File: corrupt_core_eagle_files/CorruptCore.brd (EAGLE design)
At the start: 100 x 58 mm, 90 parts, among them K1 DTS-3, K10 DTS-3, K11 DTS-3, K12 DTS-3, K13 DTS-3, K14 DTS-3, K15 DTS-3, K16 DTS-3, K2 DTS-3, K3 DTS-3, K4 DTS-3, K5 DTS-3, K6 DTS-3, K7 DTS-3, K8 DTS-3, K9 DTS-3, U1 MEGA8-P, U2 SNX4HC595SOIC16, U3 SNX4HC595SOIC16, U4 SNX4HC595SOIC16, U5 ULN2803ASOIC18, U6 ULN2803ASOIC18, U7 ULN2803ASOIC18, U8 LTC1799, Y1 16MHz

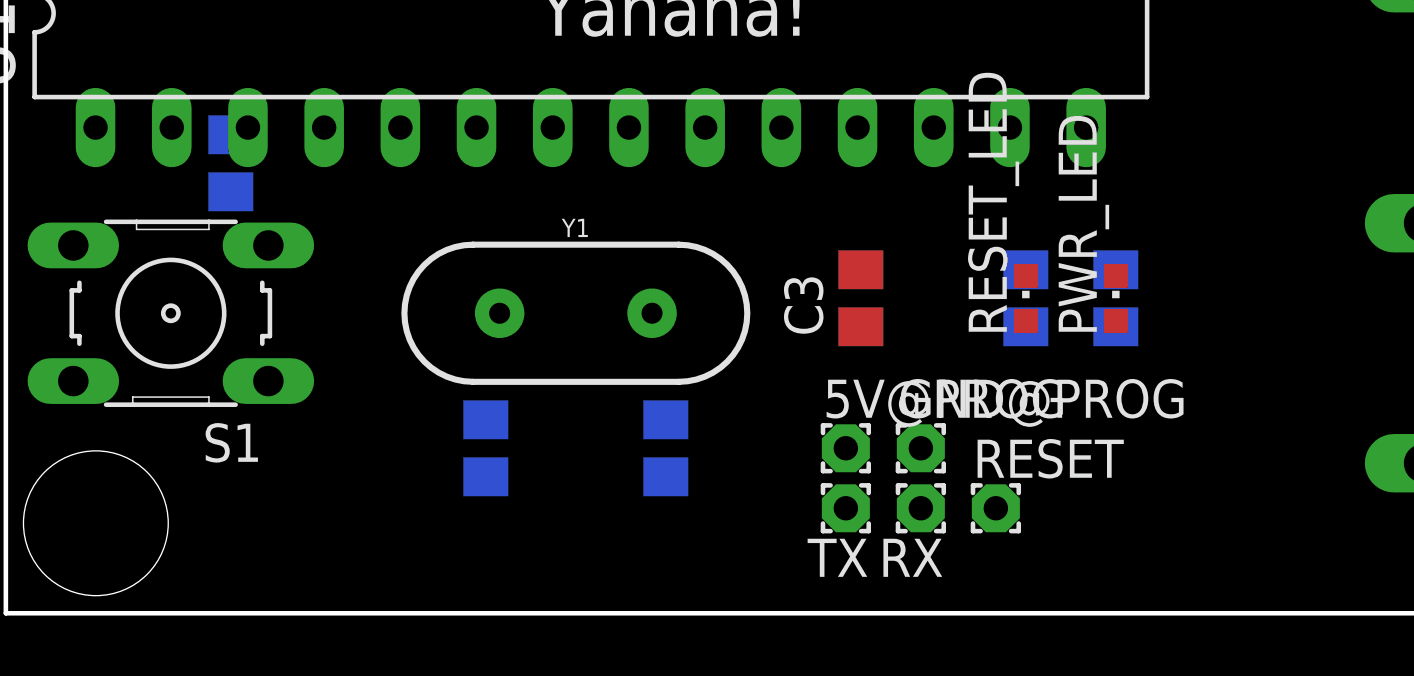
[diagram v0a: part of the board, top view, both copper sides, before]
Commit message: -starting to fix up the soldermask
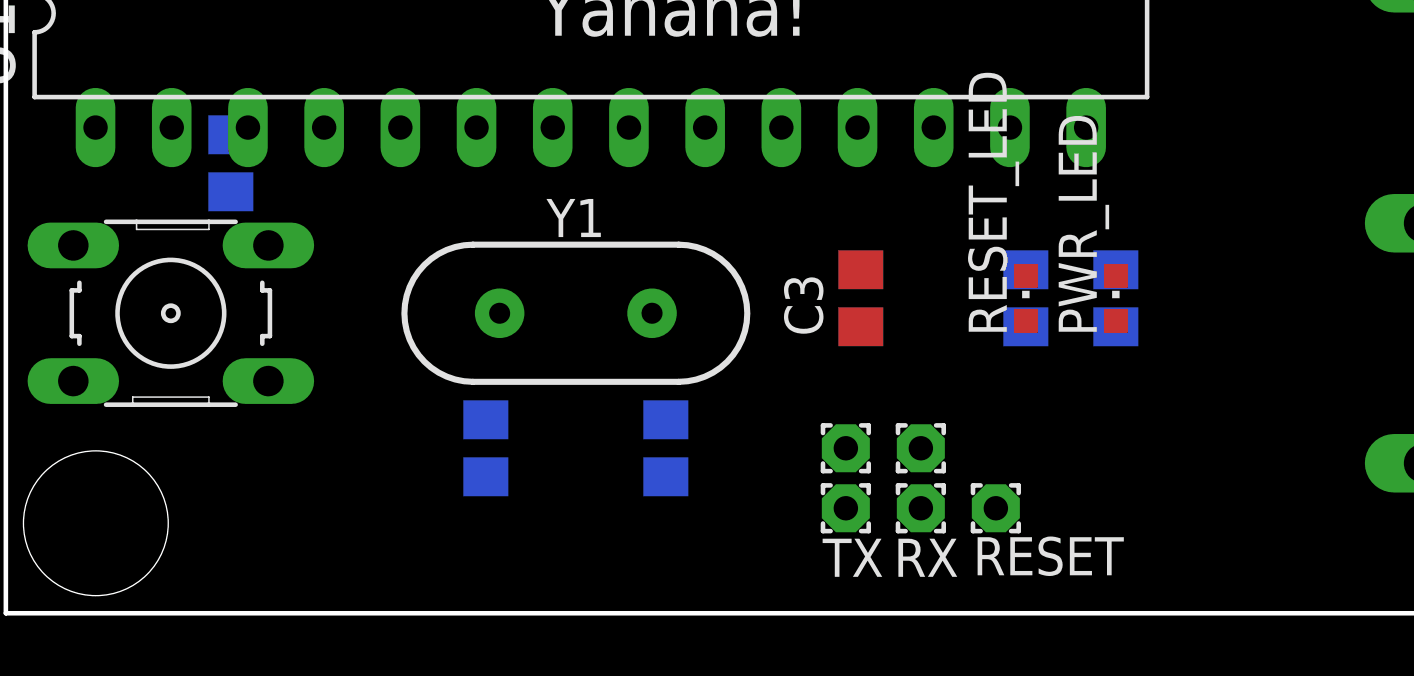
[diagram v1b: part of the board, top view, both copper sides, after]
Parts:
- 5V@PROG: value (none) -> 5V
- GND@PROG: value (none) -> GND
- S1: value (none) -> RESET
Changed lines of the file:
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@@
 <layer number="14" name="Route14" color="1" fill="6" visible="no" active="no"/>
 <layer number="15" name="Route15" color="4" fill="6" visible="no" active="no"/>
-<layer number="16" name="Bottom" color="1" fill="1" visible="yes" active="yes"/>
+<layer number="16" name="Bottom" color="1" fill="1" visible="no" active="yes"/>
 <layer number="17" name="Pads" color="2" fill="1" visible="yes" active="yes"/>
 <layer number="18" name="Vias" color="2" fill="1" visible="yes" active="yes"/>
@@
 <layer number="20" name="Dimension" color="15" fill="1" visible="yes" active="yes"/>
 <layer number="21" name="tPlace" color="7" fill="1" visible="yes" active="yes"/>
-<layer number="22" name="bPlace" color="7" fill="1" visible="yes" active="yes"/>
+<layer number="22" name="bPlace" color="7" fill="1" visible="no" active="yes"/>
 <layer number="23" name="tOrigins" color="15" fill="1" visible="yes" active="yes"/>
-<layer number="24" name="bOrigins" color="15" fill="1" visible="yes" active="yes"/>
+<layer number="24" name="bOrigins" color="15" fill="1" visible="no" active="yes"/>
 <layer number="25" name="tNames" color="7" fill="1" visible="yes" active="yes"/>
-<layer number="26" name="bNames" color="7" fill="1" visible="yes" active="yes"/>
+<layer number="26" name="bNames" color="7" fill="1" visible="no" active="yes"/>
 <layer number="27" name="tValues" color="7" fill="1" visible="yes" active="yes"/>
-<layer number="28" name="bValues" color="7" fill="1" visible="yes" active="yes"/>
+<layer number="28" name="bValues" color="7" fill="1" visible="no" active="yes"/>
 <layer number="29" name="tStop" color="7" fill="3" visible="no" active="yes"/>
 <layer number="30" name="bStop" color="7" fill="6" visible="no" active="yes"/>
@@
 <layer number="38" name="bTest" color="7" fill="1" visible="no" active="yes"/>
 <layer number="39" name="tKeepout" color="4" fill="11" visible="yes" active="yes"/>
-<layer number="40" name="bKeepout" color="1" fill="11" visible="yes" active="yes"/>
+<layer number="40" name="bKeepout" color="1" fill="11" visible="no" active="yes"/>
 <layer number="41" name="tRestrict" color="4" fill="10" visible="yes" active="yes"/>
-<layer number="42" name="bRestrict" color="1" fill="10" visible="yes" active="yes"/>
+<layer number="42" name="bRestrict" color="1" fill="10" visible="no" active="yes"/>
 <layer number="43" name="vRestrict" color="2" fill="10" visible="no" active="yes"/>
-<layer number="44" name="Drills" color="7" fill="1" visible="yes" active="yes"/>
+<layer number="44" name="Drills" color="7" fill="1" visible="no" active="yes"/>
 <layer number="45" name="Holes" color="7" fill="1" visible="yes" active="yes"/>
 <layer number="46" name="Milling" color="3" fill="1" visible="no" active="yes"/>
@@
 <layer number="50" name="dxf" color="7" fill="1" visible="no" active="no"/>
 <layer number="51" name="tDocu" color="7" fill="1" visible="yes" active="yes"/>
-<layer number="52" name="bDocu" color="7" fill="1" visible="yes" active="yes"/>
+<layer number="52" name="bDocu" color="7" fill="1" visible="no" active="yes"/>
 <layer number="53" name="tGND_GNDA" color="7" fill="9" visible="no" active="no"/>
 <layer number="54" name="bGND_GNDA" color="1" fill="9" visible="no" active="no"/>
@@
 </element>
 <element name="R1" library="resistor" library_urn="urn:adsk.eagle:library:348" package="R0805" value="10k" x="7.5" y="15" rot="MR270"/>
-<element name="S1" library="switch-omron" library_urn="urn:adsk.eagle:library:377" package="B3F-10XX" value="" x="5.5" y="10" rot="R180">
+<element name="S1" library="switch-omron" library_urn="urn:adsk.eagle:library:377" package="B3F-10XX" value="RESET" x="5.5" y="10" smashed="yes" rot="R180">
 <attribute name="MF" value="" x="5.5" y="10" size="1.778" layer="27" rot="R180" display="off"/>
 <attribute name="MPN" value="B3F-1000" x="5.5" y="10" size="1.778" layer="27" rot="R180" display="off"/>
 <attribute name="OC_FARNELL" value="176432" x="5.5" y="10" size="1.778" layer="27" rot="R180" display="off"/>
 <attribute name="OC_NEWARK" value="36M3542" x="5.5" y="10" size="1.778" layer="27" rot="R180" display="off"/>
+<attribute name="VALUE" x="10.92" y="13.048" size="1.27" layer="27" font="vector" ratio="10" rot="R270"/>
 </element>
 <element name="U2" library="CorruptCore" package="SOIC16N" value="SNX4HC595SOIC16" x="8" y="34" rot="R180"/>
@@
 <element name="U3" library="CorruptCore" package="SOIC16N" value="SNX4HC595SOIC16" x="21" y="34" rot="R180"/>
 <element name="U6" library="CorruptCore" package="SO18L" value="ULN2803ASOIC18" x="21" y="45" rot="R180"/>
-<element name="Y1" library="SparkFun-Clocks" package="HC49US" value="16MHz" x="19" y="10">
+<element name="Y1" library="SparkFun-Clocks" package="HC49US" value="16MHz" x="19" y="10" smashed="yes">
+<attribute name="NAME" x="19" y="12.54" size="1.27" layer="25" font="vector" ratio="20" align="bottom-center"/>
 <attribute name="PROD_ID" value="XTAL-08181" x="19" y="10" size="1.778" layer="27" display="off"/>
 <attribute name="SF_ID" value="COM-00536" x="19" y="10" size="1.778" layer="27" display="off"/>
+<attribute name="VALUE" x="19" y="6.96" size="1.27" layer="27" font="vector" ratio="20" align="top-center"/>
 </element>
 <element name="U4" library="CorruptCore" package="SOIC16N" value="SNX4HC595SOIC16" x="34" y="34" rot="R180"/>
@@
 <element name="R2" library="resistor" library_urn="urn:adsk.eagle:library:348" package="R0805" value="150" x="34" y="10.5" rot="MR90"/>
 <element name="R3" library="resistor" library_urn="urn:adsk.eagle:library:348" package="R0805" value="150" x="37" y="10.5" rot="MR90"/>
-<element name="C3" library="resistor" library_urn="urn:adsk.eagle:library:348" package="C0805" value="10uF" x="28.5" y="10.5" rot="R90"/>
+<element name="C3" library="resistor" library_urn="urn:adsk.eagle:library:348" package="C0805" value="10uF" x="28.5" y="10.5" smashed="yes" rot="R90">
+<attribute name="NAME" x="27.23" y="9.23" size="1.27" layer="25" font="vector" rot="R90"/>
+<attribute name="VALUE" x="31.04" y="9.23" size="1.27" layer="27" font="vector" rot="R90"/>
+</element>
 <element name="L1" library="piboy_new" package="MICROBUILDER__0805" value="10uH" x="23.5" y="28" rot="MR270"/>
 <element name="C4" library="resistor" library_urn="urn:adsk.eagle:library:348" package="C0805" value="100nF" x="20" y="28" rot="MR90"/>
-<element name="TX" library="wirepad" library_urn="urn:adsk.eagle:library:412" package="1,6/0,8" value="" x="28" y="3.5" rot="R180"/>
-<element name="RX" library="wirepad" library_urn="urn:adsk.eagle:library:412" package="1,6/0,8" value="" x="30.5" y="3.5" rot="R180"/>
-<element name="RESET" library="wirepad" library_urn="urn:adsk.eagle:library:412" package="1,6/0,8" value="" x="33" y="3.5"/>
-<element name="5V@PROG" library="wirepad" library_urn="urn:adsk.eagle:library:412" package="1,6/0,8" value="" x="28" y="5.5"/>
-<element name="GND@PROG" library="wirepad" library_urn="urn:adsk.eagle:library:412" package="1,6/0,8" value="" x="30.5" y="5.5"/>
+<element name="TX" library="wirepad" library_urn="urn:adsk.eagle:library:412" package="1,6/0,8" value="" x="28" y="3.5" smashed="yes" rot="R180">
+<attribute name="NAME" x="29.262" y="2.484" size="1.27" layer="25" font="vector" ratio="10" rot="R180"/>
+<attribute name="VALUE" x="28" y="2.9" size="0.0254" layer="27" rot="R180"/>
+</element>
+<element name="RX" library="wirepad" library_urn="urn:adsk.eagle:library:412" package="1,6/0,8" value="" x="30.5" y="3.5" smashed="yes" rot="R180">
+<attribute name="NAME" x="31.762" y="2.484" size="1.27" layer="25" font="vector" ratio="10" rot="R180"/>
+<attribute name="VALUE" x="30.5" y="2.9" size="0.0254" layer="27" rot="R180"/>
+</element>
+<element name="RESET" library="wirepad" library_urn="urn:adsk.eagle:library:412" package="1,6/0,8" value="" x="33" y="3.5" smashed="yes">
+<attribute name="NAME" x="32.238" y="1.266" size="1.27" layer="25" font="vector" ratio="10"/>
+<attribute name="VALUE" x="33" y="4.1" size="0.0254" layer="27"/>
+</element>
+<element name="5V@PROG" library="wirepad" library_urn="urn:adsk.eagle:library:412" package="1,6/0,8" value="5V" x="28" y="5.5" smashed="yes">
+<attribute name="5V" value="5v" x="27" y="6.5" size="1.27" layer="27" font="vector" display="name"/>
+<attribute name="NAME" x="27.238" y="6.516" size="1.27" layer="25" font="vector" ratio="10" display="off"/>
+<attribute name="VALUE" x="28" y="6.1" size="0.0254" layer="27"/>
+</element>
+<element name="GND@PROG" library="wirepad" library_urn="urn:adsk.eagle:library:412" package="1,6/0,8" value="GND" x="30.5" y="5.5" smashed="yes">
+<attribute name="GND" value="GND" x="29.75" y="6.5" size="1.27" layer="27" font="vector" display="name"/>
+<attribute name="NAME" x="29.738" y="6.516" size="1.27" layer="25" ratio="10" display="off"/>
+<attribute name="VALUE" x="30.5" y="6.1" size="0.0254" layer="27"/>
+</element>
 <element name="GND@POT1" library="wirepad" library_urn="urn:adsk.eagle:library:412" package="1,6/0,8" value="" x="96" y="27.5"/>
 <element name="5V@POT1" library="wirepad" library_urn="urn:adsk.eagle:library:412" package="1,6/0,8" value="" x="96" y="32.5"/>

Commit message: -more silkscreen changes
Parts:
- moved PWR_LED 8.33 mm to (42.5, 4.25)
- moved RESET_LED 8.33 mm to (39.5, 4.25)
- moved C3 0.75 mm to (28.5, 11.2)
